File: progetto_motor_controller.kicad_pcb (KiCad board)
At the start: 2 copper layers, 98 parts, among them J1 USB_B_Micro, J2 Conn_01x06, J3 Conn_01x04, J4 Screw_Terminal_01x03, J5 Conn_01x05, J6 Conn_02x10_Counter_Clockwise, J7 Conn_01x02, J8 Screw_Terminal_01x02, Q1 BSC022N04LSATMA1, Q2 BSC022N04LSATMA1, Q3 BSC022N04LSATMA1, Q4 BSC022N04LSATMA1, Q5 BSC022N04LSATMA1, Q6 BSC022N04LSATMA1, Q7 BSC022N04LSATMA1, Q8 AO3401A, SW1 SW_SPDT, U1 STM32F303RETx, U2 SN65HVD253D, U3 USBLC6-2P6, U4 TMC6140, U5 TSC2011, U6 TSC2011, U7 MYRGC07506_1, U8 TLV707, Y1 16MHz

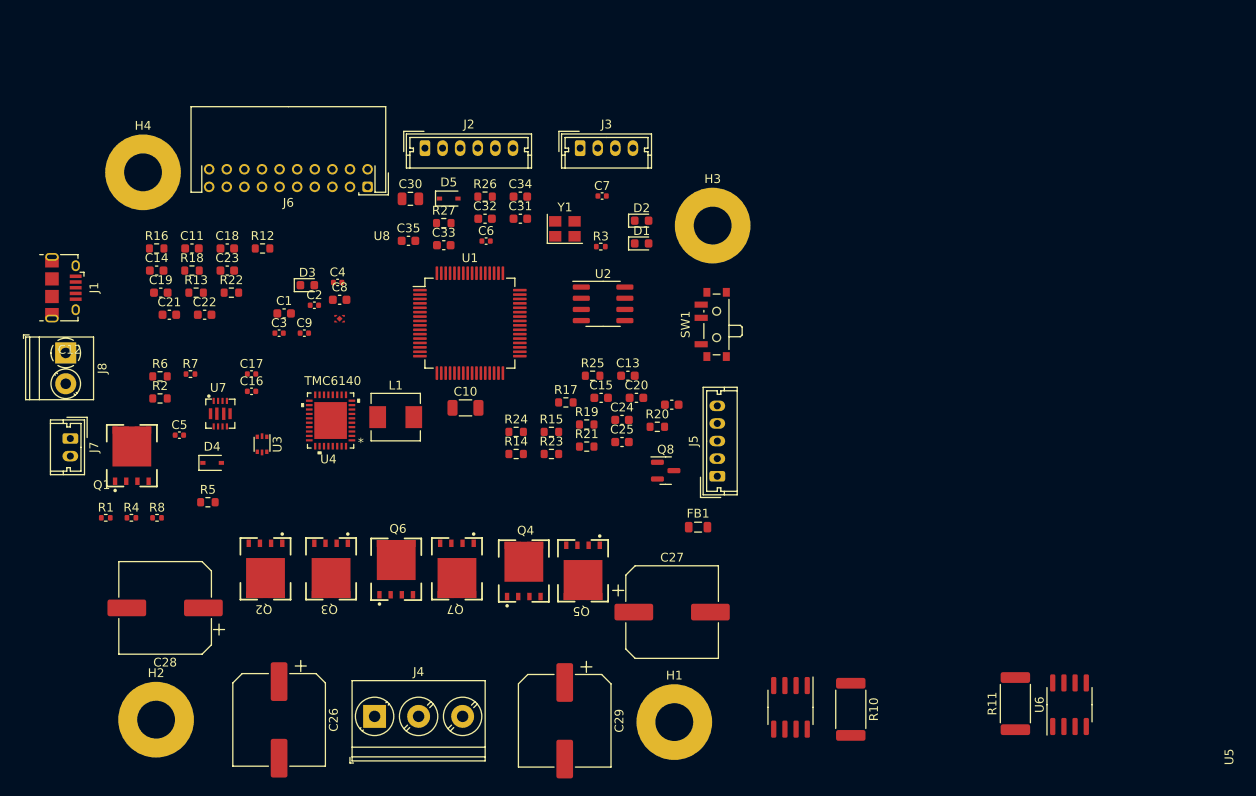
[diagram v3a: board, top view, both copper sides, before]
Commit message: started pcb layout
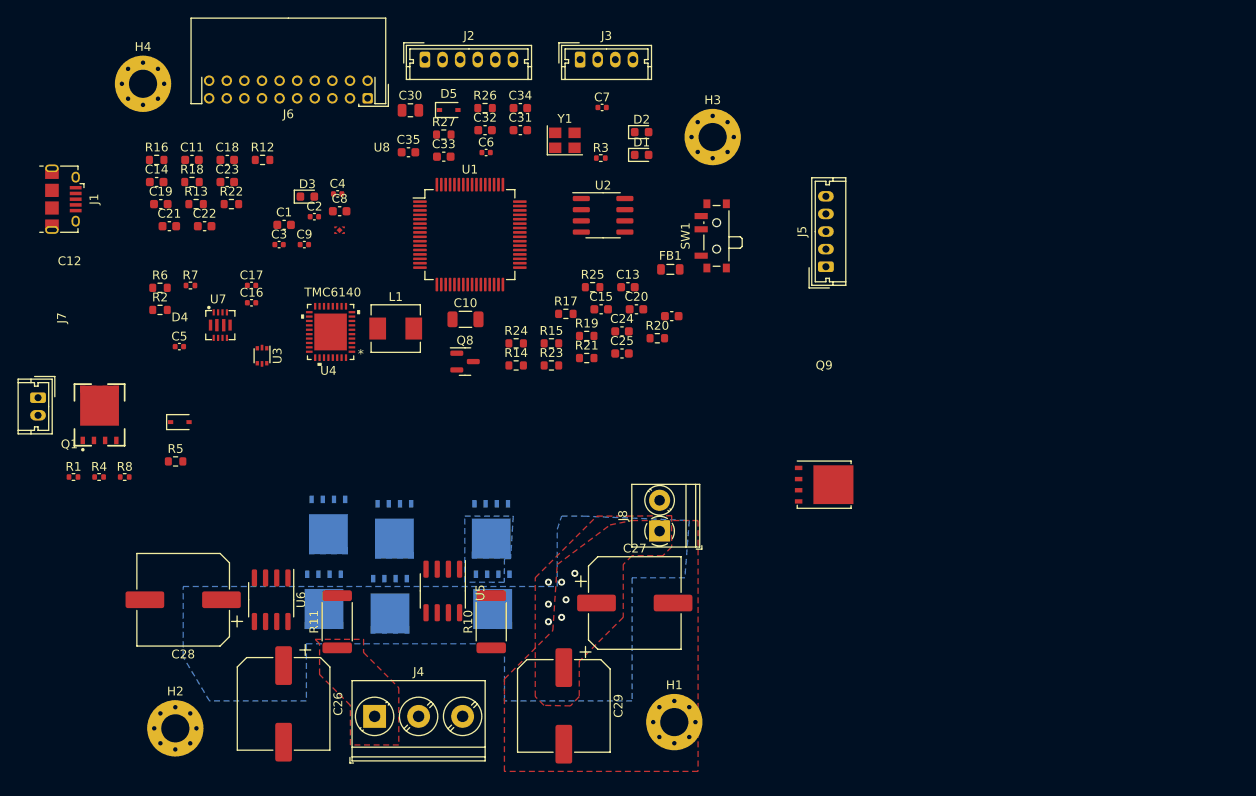
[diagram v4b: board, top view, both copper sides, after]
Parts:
- added Q9: BSC040N10NS5, Package_TO_SOT_SMD:TDSON-8-1, F.Cu at (162.3, 117.4)
- H1, H2, H3, H4: footprint MountingHole:MountingHole_4.3mm_M4_Pad -> MountingHole:MountingHole_3.2mm_M3_Pad_Via
- Q2, Q3, Q4, Q5, Q6, Q7: moved to B.Cu
- moved U6 91.5 mm to (99.5, 130.5), turned to -90 degrees
- moved R11 77.6 mm to (107.0, 133.0)
- moved J8 70.4 mm to (143.6, 122.7), turned to 90 degrees
- moved R10 42.0 mm to (124.5, 133.0), turned to 90 degrees
- moved U5 41.7 mm to (119.0, 129.5)
- moved FB1 29.5 mm to (144.8, 93.0)
- moved Q5 29.4 mm to (106.0, 122.0), turned to 0 degrees
- moved J5 26.8 mm to (162.5, 92.7)
- moved Q2 26.1 mm to (124.7, 130.5), turned to 0 degrees
- moved Q8 25.9 mm to (121.5, 103.4)
- moved Q4 22.9 mm to (105.5, 130.5)
- moved Q3 18.7 mm to (124.5, 122.5), turned to 0 degrees
- moved C1 10.1 mm to (101.0, 87.9)
- moved C10 10.1 mm to (121.6, 98.6)
- moved C11 10.1 mm to (90.5, 80.5)
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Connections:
- C26 pad 2: Net-(C26-Pad2) -> GND
- C27 pad 2: Net-(C26-Pad2) -> GND
- C28 pad 2: Net-(C26-Pad2) -> GND
- C29 pad 2: Net-(C26-Pad2) -> GND
- J4 pad 1: PH_A -> PH_B
- J4 pad 2: PH_B -> PH_A
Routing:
- net VDD: vias 0 -> 7
- added copper zone on F.Cu, net GND
- added copper zone on B.Cu, net PH_A_CS
- added copper zone on F.Cu, net PH_B
- added copper zone on B.Cu, net VDD
- added copper zone on F.Cu, net VDD
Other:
- copper layers 2 -> 4

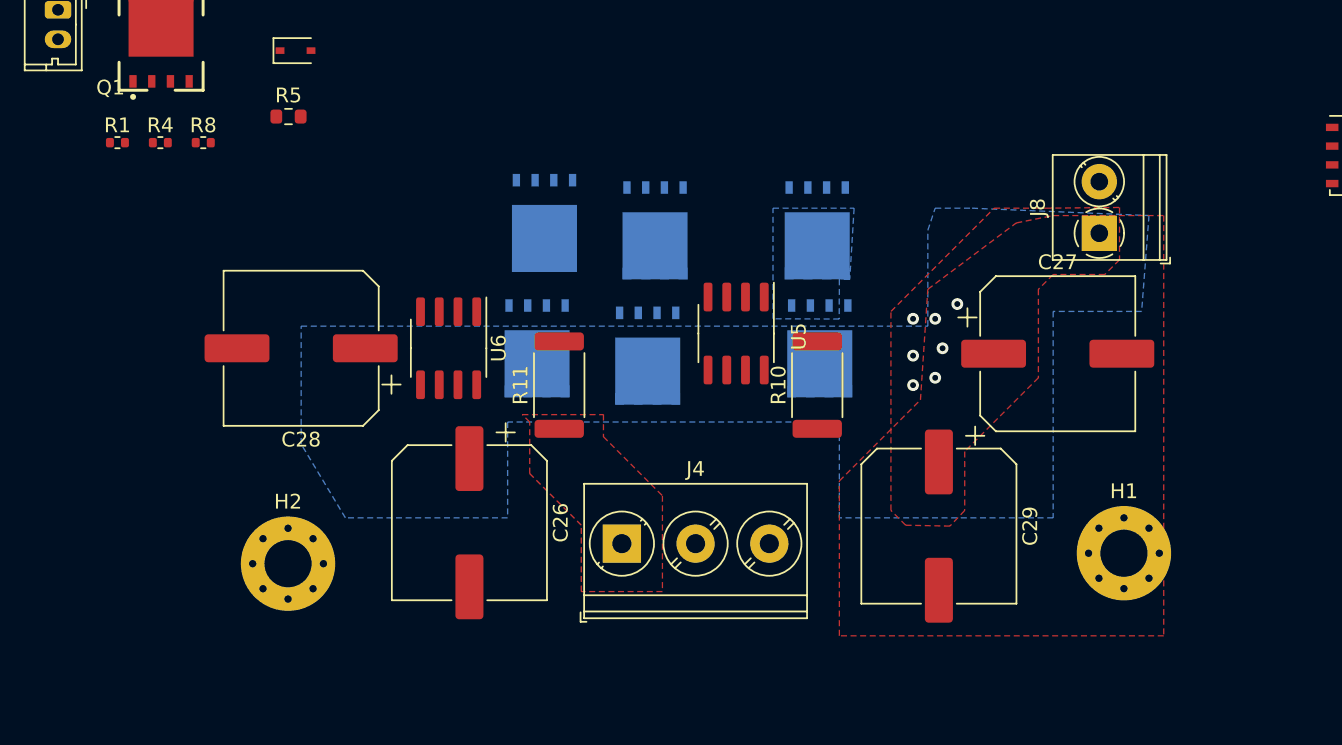
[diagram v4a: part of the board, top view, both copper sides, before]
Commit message: added capacitor footprints
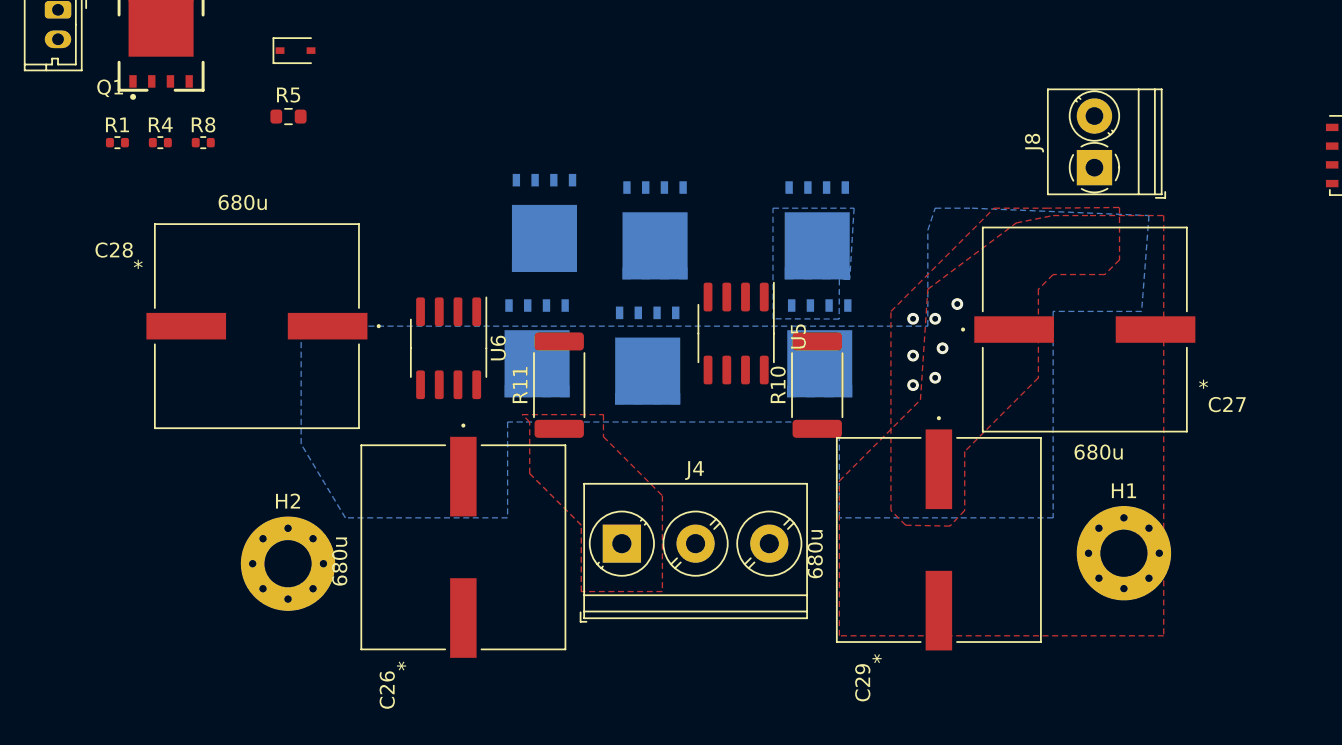
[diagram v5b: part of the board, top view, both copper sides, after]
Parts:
- C26, C27, C28, C29: footprint Capacitor_SMD:CP_Elec_10x12.6 -> MyLibrary:Electrolytic_Cap_12.5x13.5
- moved J8 4.46 mm to (143.3, 118.2)
- moved C28 3.35 mm to (86.5, 129.0)
- moved C27 2.46 mm to (142.6, 129.2)
- moved C26 1.72 mm to (100.5, 144.0)
- moved C29 0.94 mm to (132.8, 143.5)

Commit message: rev_0.1
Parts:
- removed D3: LED_Small, LED_SMD:LED_0603_1608Metric
- removed FB1: 600 @ 600MHz, Inductor_SMD:L_0805_2012Metric
- removed Q9: BSC040N10NS5, Package_TO_SOT_SMD:TDSON-8-1
- removed R6: 1k5, Resistor_SMD:R_0603_1608Metric
- removed SW1: SW_SPDT, Button_Switch_SMD:SW_SPDT_PCM12
- added C36: 1u, Capacitor_SMD:C_0603_1608Metric, F.Cu at (127.8, 97.6)
- added C37: 1u, Capacitor_SMD:C_0603_1608Metric, F.Cu at (124.5, 96.7)
- added C38: 22u, Capacitor_SMD:C_0603_1608Metric, F.Cu at (96.0, 102.5)
- added C39: 2u2, Capacitor_SMD:C_0603_1608Metric, F.Cu at (129.2, 107.8)
- added C40: 2u2, Capacitor_SMD:C_0603_1608Metric, F.Cu at (138.3, 104.4)
- added C41: 2u2, Capacitor_SMD:C_0603_1608Metric, F.Cu at (129.2, 103.2)
- added C42: 1u, Capacitor_SMD:C_0402_1005Metric, B.Cu at (110.5, 101.1)
- added C43: 10n, Capacitor_SMD:C_0402_1005Metric, B.Cu at (111.6, 101.1)
- added D6: UDZVFH10B, Diode_SMD:D_SOD-323_HandSoldering, F.Cu at (135.8, 118.5)
- added J9: Conn_01x03, Connector_PinHeader_2.54mm:PinHeader_1x03_P2.54mm_Vertical, F.Cu at (101.5, 81.7)
- added NTC1: 10k, Resistor_SMD:R_0603_1608Metric, F.Cu at (107.1, 107.7)
- added R28: 120k, Resistor_SMD:R_0603_1608Metric, F.Cu at (139.8, 118.5)
- added R29: 1k5, Resistor_SMD:R_0603_1608Metric, F.Cu at (127.7, 103.2)
- added R30: 1k5, Resistor_SMD:R_0603_1608Metric, F.Cu at (136.5, 104.4)
- added R31: 1k5, Resistor_SMD:R_0603_1608Metric, F.Cu at (127.3, 107.8)
- added R32: 1k5, Resistor_SMD:R_0603_1608Metric, F.Cu at (130.8, 107.8)
- added R33: 1k5, Resistor_SMD:R_0603_1608Metric, F.Cu at (140.1, 104.4)
- added R34: 1k5, Resistor_SMD:R_0603_1608Metric, F.Cu at (130.9, 103.5)
- added R9: 10k, Resistor_SMD:R_0603_1608Metric, F.Cu at (107.1, 106.0)
- added U9: TLV707, MyLibrary:TLV707, F.Cu at (126.2, 97.1)
- C10: value 47u -> 22u; footprint Capacitor_SMD:C_1206_3216Metric -> Capacitor_SMD:C_0603_1608Metric
- C16, C17, C19, C21, C22, C24, C31, C32, R10, R11, R13, R18, R19, R20, R21, R22, R23, U5, U6, U8: moved to B.Cu
- J2: footprint Connector_Molex:Molex_Micro-Latch_53253-0670_1x06_P2.00mm_Vertical -> Connector_JST_mod:JST_GH_SM06B-GHS-TB_06x1.25mm_Angled
- J3: footprint Connector_Molex:Molex_Micro-Latch_53253-0470_1x04_P2.00mm_Vertical -> Connector_JST_mod:JST_GH_SM04B-GHS-TB_04x1.25mm_Angled
- J5: footprint Connector_Molex:Molex_Micro-Latch_53253-0570_1x05_P2.00mm_Vertical -> Connector_JST_mod:JST_GH_SM05B-GHS-TB_05x1.25mm_Angled
- J6: value Conn_02x10_Counter_Clockwise -> Conn_02x10_Odd_Even; footprint Connector_JST:JST_PHD_S20B-PHDSS_2x10_P2.00mm_Horizontal -> MyLibrary:JST_SHD_SM20B
- J7: footprint Connector_Molex:Molex_Micro-Latch_53253-0270_1x02_P2.00mm_Vertical -> Connector_JST_mod:JST_GH_SM02B-GHS-TB_02x1.25mm_Angled
- L1: footprint Inductor_SMD:L_Sunlord_MWSA0518_5.4x5.2mm -> Inductor_SMD:L_1210_3225Metric
- Q1: footprint MyLibrary:TDSON-8-6_copy -> Package_TO_SOT_SMD:SOT-23
- Q2, Q3, Q4, Q5, Q6, Q7: moved to F.Cu
- Q8: value AO3401A -> BSC022N04LSATMA1; footprint Package_TO_SOT_SMD:SOT-23 -> MyLibrary:TDSON-8-6_copy
- R1, R4, R7, R8: footprint Resistor_SMD:R_0402_1005Metric -> Resistor_SMD:R_0603_1608Metric
- U3: footprint Package_TO_SOT_SMD:SOT-666 -> Package_TO_SOT_SMD:SOT-363_SC-70-6
- moved J7 74.2 mm to (145.5, 91.5), turned to 90 degrees
- moved Q1 63.3 mm to (140.1, 89.5), turned to 180 degrees
- moved R8 60.3 mm to (136.6, 89.2), turned to 90 degrees
- moved C23 59.5 mm to (131.0, 130.0)
- moved R16 58.6 mm to (122.6, 126.7), turned to 90 degrees
- moved J1 58.2 mm to (133.9, 79.9), turned to 180 degrees
- moved D2 56.1 mm to (89.3, 97.7)
- moved D1 55.9 mm to (89.3, 99.7)
- moved C12 54.5 mm to (93.9, 117.2)
- moved C16 53.9 mm to (136.2, 134.1), turned to 180 degrees
- moved D4 53.8 mm to (140.0, 92.9), turned to 180 degrees
- moved R4 53.5 mm to (123.2, 85.0), turned to 180 degrees
- moved J3 52.8 mm to (86.8, 91.5), turned to -90 degrees
- moved C20 51.4 mm to (100.8, 129.6), turned to 180 degrees
- moved R22 47.3 mm to (131.2, 116.0), turned to 180 degrees
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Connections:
- net Net-(C12-Pad1) renamed /Inverter/V10
- net Net-(C33-Pad2) renamed /Power/FB
- net Net-(L1-Pad2) renamed /Inverter/SW
- net Net-(U7-Pad1) renamed /Power/LX
- C10 pad 1: 3V3_MCU -> 3V3_TMC
- C14 pad 1: PH_B_CS -> PH_B
- C15 pad 1: PH_C -> PH_C_CS
- C20 pad 2: Net-(C20-Pad2) -> GND
- C22 pad 1: V_EMF_SENSE_C -> V_EMF_SENSE_A
- C23 pad 2: Net-(C20-Pad2) -> GND
- C24 pad 1: V_EMF_SENSE_A -> V_EMF_SENSE_C
- C25 pad 2: Net-(C20-Pad2) -> GND
- D5 pad 1: V_SUPPLY -> VDD
- D5 pad 2: GND -> V_SUPPLY-
- J3 pad 3: CAN_H -> CAN_L
- J3 pad 4: CAN_L -> CAN_H
- J4 pad 1: PH_B -> PH_C
- J4 pad 2: PH_A -> PH_B
- J4 pad 3: PH_C -> PH_A
- J5 pad 1: 5V -> GND
- J5 pad 2: ENC_A -> /ENC_AA
- J5 pad 3: ENC_B -> /ENC_BB
- J5 pad 4: ENC_I -> /ENC_II
- J5 pad 5: GND -> 5V
- J6 pad 1: 5V -> GND
- J6 pad 10: GND -> ERROR
- J6 pad 11: GND -> UART_RX
- J6 pad 12: GND -> PWM_IN_1
- J6 pad 13: GND -> EN
- J6 pad 15: PWM_IN_1 -> GND
- J6 pad 16: NSS -> GND
- J6 pad 17: SCK -> GND
- J6 pad 18: UART_TX -> 3V3_MCU
- J6 pad 2: 3V3_MCU -> 5V
- J6 pad 20: GND -> 5V
- J6 pad 3: UART_RX -> GND
- J6 pad 4: MISO -> 3V3_MCU
- J6 pad 5: MOSI -> MISO
- J6 pad 6: ERROR -> NSS
- J6 pad 7: ENABLE -> MOSI
- J6 pad 8: 3V3_MCU -> SCK
- J6 pad 9: 5V -> UART_TX
- J8 pad 1: V_SUPPLY -> VDD
- J8 pad 2: GND -> V_SUPPLY-
- L1 pad 1: 3V3_MCU -> 3V3_TMC
- Q2 pad 2: /Inverter/HA_G -> /Inverter/HC_G
- Q2 pad 3: PH_A_CS -> PH_C_CS
- Q3 pad 1: PH_A_CS -> PH_C_CS
- Q3 pad 2: /Inverter/LA_G -> /Inverter/LC_G
- Q4 pad 2: /Inverter/HB_G -> /Inverter/HA_G
- Q4 pad 3: PH_B_CS -> PH_A_CS
- Q5 pad 1: PH_B_CS -> PH_A_CS
- Q5 pad 2: /Inverter/LB_G -> /Inverter/LA_G
- Q6 pad 2: /Inverter/HC_G -> /Inverter/HB_G
- Q6 pad 3: PH_C -> PH_B
- Q7 pad 1: PH_C -> PH_B
- Q7 pad 2: /Inverter/LC_G -> /Inverter/LB_G
- Q8 pad 1: GND -> V_SUPPLY-
- Q8 pad 3: V_SUPPLY -> GND
- R10 pad 1: PH_A -> PH_C
- R10 pad 2: PH_A_CS -> PH_C_CS
- R11 pad 1: PH_B -> PH_A
- R11 pad 2: PH_B_CS -> PH_A_CS
- R14 pad 1: /Inverter/HA_G -> /Inverter/HC_G
- R14 pad 2: HA -> HC
- R15 pad 1: /Inverter/LA_G -> /Inverter/LC_G
- R15 pad 2: LA -> LC
- R16 pad 1: /Inverter/HB_G -> /Inverter/HA_G
- R16 pad 2: HB -> HA
- R17 pad 1: /Inverter/LB_G -> /Inverter/LA_G
- R17 pad 2: LB -> LA
- R19 pad 1: PH_C -> PH_A_CS
- R19 pad 2: V_EMF_SENSE_C -> V_EMF_SENSE_A
- R20 pad 1: PH_A -> PH_C_CS
- R20 pad 2: V_EMF_SENSE_A -> V_EMF_SENSE_C
- R22 pad 1: V_EMF_SENSE_C -> V_EMF_SENSE_A
- R23 pad 1: V_EMF_SENSE_A -> V_EMF_SENSE_C
- R24 pad 1: /Inverter/HC_G -> /Inverter/HB_G
- R24 pad 2: HC -> HB
- R25 pad 1: /Inverter/LC_G -> /Inverter/LB_G
- R25 pad 2: LC -> LB
- U1 pad 10: PWM_HC -> PWM_HA
- U1 pad 23: PWM_LA -> PWM_LC
- U1 pad 27: PWM_LC -> PWM_LA
- U1 pad 42: LED_B -> unconnected-(U1-Pad42)
- U1 pad 8: PWM_HA -> PWM_HC
- U4 pad 21: 3V3_MCU -> 3V3_TMC
- U4 pad 36: PH_C -> PH_C_CS
- U4 pad 4: PH_B_CS -> PH_B
- U5 pad 1: PH_A_CS -> PH_C_CS
- U5 pad 8: PH_A -> PH_C
- U6 pad 1: PH_B_CS -> PH_A_CS
- U6 pad 8: PH_B -> PH_A
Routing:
- net 3V3_MCU: track 0.00 -> 87.8 mm, vias 0 -> 6
- net GND: track 0.00 -> 84.5 mm, vias 0 -> 318
- net 3V3_VDAA: track 0.00 -> 75.8 mm, vias 0 -> 6
- net /Inverter/C1_OUT: track 0.00 -> 65.2 mm
- net VDD: track 0.00 -> 64.5 mm, vias 7 -> 105
- net HA: track 0.00 -> 44.8 mm, vias 0 -> 2
- net PH_A_CS: track 0.00 -> 41.6 mm, vias 0 -> 29
- net ENABLE: track 0.00 -> 41.1 mm, vias 0 -> 2
- net DIAG: track 0.00 -> 38.2 mm, vias 0 -> 2
- net LA: track 0.00 -> 36.9 mm
- net SH_SET: track 0.00 -> 33.9 mm, vias 0 -> 2
- net PWM_LC: track 0.00 -> 33.8 mm, vias 0 -> 2
- net FAN_PWM: track 0.00 -> 33.5 mm, vias 0 -> 2
- net /Inverter/C2_OUT: track 0.00 -> 33.4 mm, vias 0 -> 1
- net 5V: track 0.00 -> 33.4 mm, vias 0 -> 15
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- added copper zone on F.Cu, net /Inverter/SW
- added copper zone on F.Cu, net /Power/FB
- added copper zone on F.Cu, net /Power/LX
- added copper zone on B.Cu, net 3V3_MCU
- added copper zone on F.Cu, net 3V3_MCU
- added copper zone on F.Cu, net 3V3_TMC
- added copper zone on B.Cu, net 3V3_VDAA
- added copper zone on In2.Cu, net 3V3_VDAA
- added copper zone on B.Cu, net 5V
- added copper zone on F.Cu, net 5V
- added copper zone on In2.Cu, net 5V
- added copper zone on B.Cu, net GND
- added copper zone on In1.Cu, net GND
- added copper zone on In2.Cu, net GND
- added copper zone on B.Cu, net PH_A
- added copper zone on In2.Cu, net PH_A
- added copper zone on F.Cu, net PH_A_CS
- added copper zone on B.Cu, net PH_B
- added copper zone on In2.Cu, net PH_B
- added copper zone on B.Cu, net PH_C
- added copper zone on In2.Cu, net PH_C
- added copper zone on B.Cu, net PH_C_CS
- added copper zone on F.Cu, net PH_C_CS
- added copper zone on In1.Cu, net VDD
- added copper zone on F.Cu, net V_SUPPLY-
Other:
- board outline added: 66 x 75 mm
- rule pad_to_mask_clearance: 0 -> 0.05

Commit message: branch test
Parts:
- moved R1 4.25 mm to (101.9, 87.9)
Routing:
- net Net-(R1-Pad2): track 2.49 -> 7.08 mm
- net BOOT0: track 17.6 -> 14.1 mm
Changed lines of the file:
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@@
   )
   (footprint "Resistor_SMD:R_0603_1608Metric" (layer "F.Cu")
-    (at 100 84.1 180)
+    (at 101.9 87.9 180)
     (descr "Resistor SMD 0603 (1608 Metric), square (rectangular) end terminal, IPC_7351 nominal, (Body size source: IPC-SM-782 page 72, https://www.pcb-3d.com/wordpress/wp-content/uploads/ipc-sm-782a_amendment_1_and_2.pdf), generated with kicad-footprint-generator")
     (tags "resistor")
@@
   (segment (start 100.75 131.15) (end 100.75 131.9625) (width 0.25) (layer "B.Cu") (net 19))
   (segment (start 94.1 129.5) (end 99.1 129.5) (width 0.25) (layer "B.Cu") (net 19))
-  (segment (start 113.05 92.45) (end 105.6 85) (width 0.2) (layer "F.Cu") (net 20))
-  (segment (start 105.6 85) (end 101.725 85) (width 0.2) (layer "F.Cu") (net 20))
-  (segment (start 101.725 85) (end 100.825 84.1) (width 0.2) (layer "F.Cu") (net 20))
+  (segment (start 108.5 87.9) (end 102.725 87.9) (width 0.2) (layer "F.Cu") (net 20))
+  (segment (start 113.05 92.45) (end 108.5 87.9) (width 0.2) (layer "F.Cu") (net 20))
   (segment (start 113.05 94.325) (end 113.05 92.45) (width 0.2) (layer "F.Cu") (net 20))
-  (segment (start 99.175 84.1) (end 99.175 81.915) (width 0.2) (layer "F.Cu") (net 21))
-  (segment (start 99.175 81.915) (end 98.96 81.7) (width 0.2) (layer "F.Cu") (net 21))
+  (segment (start 101.075 87.9) (end 101.075 83.815) (width 0.2) (layer "F.Cu") (net 21))
+  (segment (start 101.075 83.815) (end 98.96 81.7) (width 0.2) (layer "F.Cu") (net 21))
   (segment (start 109.125 98.75) (end 107.51 98.75) (width 0.3) (layer "F.Cu") (net 22))
   (segment (start 107.51 98.75) (end 107.185 99.075) (width 0.3) (layer "F.Cu") (net 22))
